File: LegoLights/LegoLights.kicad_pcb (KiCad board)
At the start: 2 copper layers, 30.5 x 7.6 mm, 4 parts, among them J1 Conn_01x02, J2 Conn_01x02

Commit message: Update paths more thick
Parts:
- moved D1 1.02 mm to (133.9, 60.5)
- moved R1 0.51 mm to (137.2, 58.3)
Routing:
- net GND: track 20.6 -> 0.01 mm
- added copper zone on F.Cu, net GND
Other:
- board text added: "Lego Lights Rev1.0"
- board text removed: "Lego Lights"
- board text removed: "Rick Winters 2024"
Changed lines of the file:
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@@
   )
   (footprint "LED_SMD:LED_1210_3225Metric_Pad1.42x2.65mm_HandSolder" (layer "F.Cu")
-    (at 133.858 59.4725 90)
+    (at 133.858 60.4885 90)
     (descr "LED SMD 1210 (3225 Metric), square (rectangular) end terminal, IPC_7351 nominal, (Body size source: http://www.tortai-tech.com/upload/download/2011102023233369053.pdf), generated with kicad-footprint-generator")
     (tags "LED handsolder")
@@
     (property "ki_keywords" "LED diode")
     (attr smd)
-    (fp_text reference "D1" (at 0 -2.28 90) (layer "F.SilkS")
+    (fp_text reference "D1" (at 0 -2.54 180) (layer "F.SilkS")
         (effects (font (size 1 1) (thickness 0.15)))
     )
@@
   )
   (footprint "Resistor_SMD:R_0805_2012Metric" (layer "F.Cu")
-    (at 137.16 58.7775 -90)
+    (at 137.16 58.2695 -90)
     (descr "Resistor SMD 0805 (2012 Metric), square (rectangular) end terminal, IPC_7351 nominal, (Body size source: IPC-SM-782 page 72, https://www.pcb-3d.com/wordpress/wp-content/uploads/ipc-sm-782a_amendment_1_and_2.pdf), generated with kicad-footprint-generator")
     (tags "resistor")
@@
     (property "ki_keywords" "R res resistor")
     (attr smd)
-    (fp_text reference "R1" (at 0 -1.65 90) (layer "F.SilkS")
+    (fp_text reference "R1" (at 0 -2.032 -180) (layer "F.SilkS")
         (effects (font (size 1 1) (thickness 0.15)))
     )
@@
   (gr_rect (start 119.38 55.88) (end 149.86 63.5)
     (stroke (width 0.2) (type default)) (fill none) (layer "Edge.Cuts"))
-  (gr_text "Lego Lights" (at 139.192 57.912) (layer "B.SilkS")
-    (effects (font (size 1 1) (thickness 0.15)) (justify left bottom mirror))
-  )
-  (gr_text "Rick Winters 2024" (at 141.986 61.214) (layer "B.SilkS")
+  (gr_text "Lego Lights Rev1.0" (at 141.478 60.452) (layer "B.SilkS")
     (effects (font (size 1 1) (thickness 0.15)) (justify left bottom mirror))
   )
@@
     (effects (font (size 1 1) (thickness 0.15)) (justify left bottom))
   )
-  (gr_text "GND" (at 139.954 61.468) (layer "F.SilkS")
+  (gr_text "GND" (at 140.208 61.722) (layer "F.SilkS")
     (effects (font (size 1 1) (thickness 0.15)) (justify left bottom))
   )
-  (gr_text "+" (at 141.478 58.928) (layer "F.SilkS")
+  (gr_text "+" (at 141.224 58.928) (layer "F.SilkS")
     (effects (font (size 1 1) (thickness 0.15)) (justify left bottom))
   )
-  (gr_text "+" (at 125.73 59.182) (layer "F.SilkS")
+  (gr_text "+" (at 126.238 58.928) (layer "F.SilkS")
     (effects (font (size 1 1) (thickness 0.15)) (justify left bottom))
   )
-  (segment (start 134.693 57.985) (end 133.858 57.985) (width 0.25) (layer "F.Cu") (net 1))
-  (segment (start 136.398 59.69) (end 134.693 57.985) (width 0.25) (layer "F.Cu") (net 1))
+  (segment (start 134.039 59.182) (end 133.858 59.001) (width 1) (layer "F.Cu") (net 1))
+  (segment (start 137.16 59.182) (end 134.039 59.182) (width 1) (layer "F.Cu") (net 1))
   (segment (start 133.858 58.42) (end 134.7235 58.42) (width 0.25) (layer "F.Cu") (net 1))
   (segment (start 144.78 60.99) (end 144.77 60.98) (width 0.25) (layer "F.Cu") (net 2))
-  (segment (start 144.77 60.98) (end 124.186 60.98) (width 0.25) (layer "F.Cu") (net 2))
-  (segment (start 137.16 57.865) (end 135.937 56.642) (width 0.25) (layer "F.Cu") (net 3))
-  (segment (start 137.745 58.45) (end 137.16 57.865) (width 0.25) (layer "F.Cu") (net 3))
-  (segment (start 132.334 56.642) (end 130.536 58.44) (width 0.25) (layer "F.Cu") (net 3))
-  (segment (start 144.78 58.45) (end 137.745 58.45) (width 0.25) (layer "F.Cu") (net 3))
-  (segment (start 130.536 58.44) (end 124.186 58.44) (width 0.25) (layer "F.Cu") (net 3))
-  (segment (start 144.78 58.45) (end 144.75 58.42) (width 0.25) (layer "F.Cu") (net 3))
-  (segment (start 135.937 56.642) (end 132.334 56.642) (width 0.25) (layer "F.Cu") (net 3))
+  (segment (start 144.78 58.45) (end 143.48 57.15) (width 0.75) (layer "F.Cu") (net 3))
+  (segment (start 125.431 57.15) (end 124.181 58.4) (width 0.75) (layer "F.Cu") (net 3))
+  (segment (start 143.48 57.15) (end 125.431 57.15) (width 0.75) (layer "F.Cu") (net 3))
+  (zone (net 2) (net_name "GND") (layer "F.Cu") (hatch edge 0.5)
+    (connect_pads (clearance 0.5))
+    (min_thickness 0.25) (filled_areas_thickness no)
+    (fill yes (thermal_gap 0.5) (thermal_bridge_width 0.5))
+    (polygon
+      (pts
+        (xy 149.86 55.88)
+        (xy 119.38 55.88)
+        (xy 119.38 63.5)
+        (xy 149.86 63.5)
+        (xy 149.86 55.88)
+      )
+    )
+  )
 )

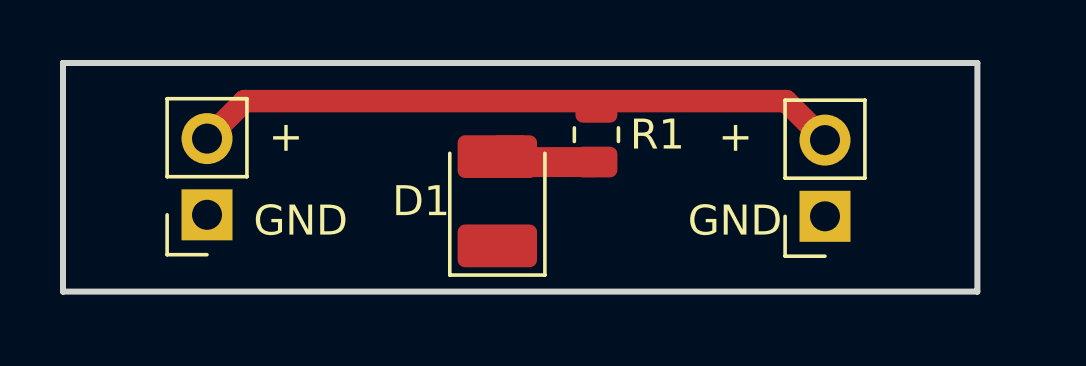
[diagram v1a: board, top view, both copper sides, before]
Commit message: Update dimensions to correct size of a lego 1x4
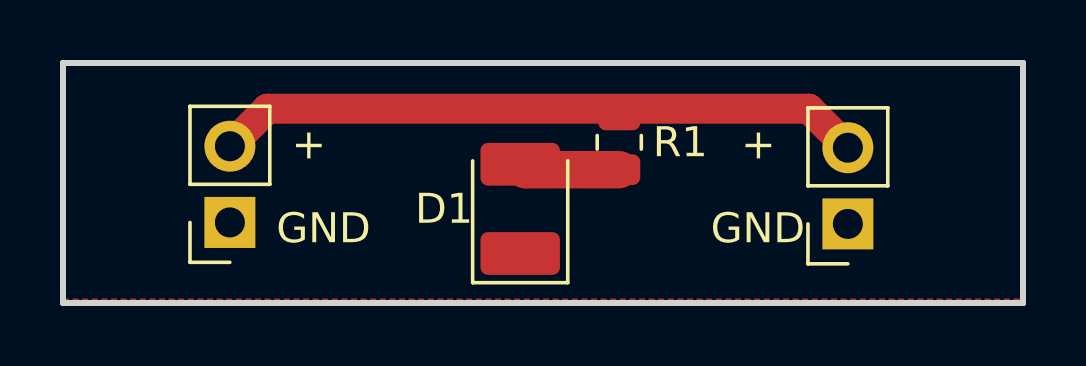
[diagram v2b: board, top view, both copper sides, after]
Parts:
- moved J1 0.80 mm to (124.9, 61.2)
- moved D1 0.80 mm to (134.6, 60.7)
- moved J2 0.80 mm to (145.5, 61.2)
- moved R1 0.80 mm to (137.9, 58.5)
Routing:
- net Net-(D1-A): track 4.24 -> 3.38 mm
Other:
- board size 30.5 x 7.6 mm -> 32 x 8 mm
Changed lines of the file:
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@@
   (net 3 "+12V")
   (footprint "Connector_PinSocket_2.54mm:PinSocket_1x02_P2.54mm_Vertical" (layer "F.Cu")
-    (at 124.181 60.94 180)
+    (at 124.943 61.194 180)
     (descr "Through hole straight socket strip, 1x02, 2.54mm pitch, single row (from Kicad 4.0.7), script generated")
     (tags "Through hole socket strip THT 1x02 2.54mm single row")
@@
   )
   (footprint "LED_SMD:LED_1210_3225Metric_Pad1.42x2.65mm_HandSolder" (layer "F.Cu")
-    (at 133.858 60.4885 90)
+    (at 134.62 60.7425 90)
     (descr "LED SMD 1210 (3225 Metric), square (rectangular) end terminal, IPC_7351 nominal, (Body size source: http://www.tortai-tech.com/upload/download/2011102023233369053.pdf), generated with kicad-footprint-generator")
     (tags "LED handsolder")
@@
   )
   (footprint "Resistor_SMD:R_0805_2012Metric" (layer "F.Cu")
-    (at 137.16 58.2695 -90)
+    (at 137.922 58.5235 -90)
     (descr "Resistor SMD 0805 (2012 Metric), square (rectangular) end terminal, IPC_7351 nominal, (Body size source: IPC-SM-782 page 72, https://www.pcb-3d.com/wordpress/wp-content/uploads/ipc-sm-782a_amendment_1_and_2.pdf), generated with kicad-footprint-generator")
     (tags "resistor")
@@
   )
   (footprint "Connector_PinSocket_2.54mm:PinSocket_1x02_P2.54mm_Vertical" (layer "F.Cu")
-    (at 144.78 60.99 180)
+    (at 145.542 61.244 180)
     (descr "Through hole straight socket strip, 1x02, 2.54mm pitch, single row (from Kicad 4.0.7), script generated")
     (tags "Through hole socket strip THT 1x02 2.54mm single row")
@@
     )
   )
-  (gr_rect (start 119.38 55.88) (end 149.86 63.5)
+  (gr_rect (start 119.38 55.88) (end 151.38 63.88)
     (stroke (width 0.2) (type default)) (fill none) (layer "Edge.Cuts"))
-  (gr_text "Lego Lights Rev1.0" (at 141.478 60.452) (layer "B.SilkS")
+  (gr_text "Lego Lights Rev1.0" (at 142.24 60.706) (layer "B.SilkS")
     (effects (font (size 1 1) (thickness 0.15)) (justify left bottom mirror))
   )
-  (gr_text "GND" (at 125.73 61.722) (layer "F.SilkS")
-    (effects (font (size 1 1) (thickness 0.15)) (justify left bottom))
-  )
-  (gr_text "GND" (at 140.208 61.722) (layer "F.SilkS")
-    (effects (font (size 1 1) (thickness 0.15)) (justify left bottom))
-  )
-  (gr_text "+" (at 141.224 58.928) (layer "F.SilkS")
-    (effects (font (size 1 1) (thickness 0.15)) (justify left bottom))
-  )
-  (gr_text "+" (at 126.238 58.928) (layer "F.SilkS")
-    (effects (font (size 1 1) (thickness 0.15)) (justify left bottom))
-  )
-  (segment (start 134.039 59.182) (end 133.858 59.001) (width 1) (layer "F.Cu") (net 1))
-  (segment (start 137.16 59.182) (end 134.039 59.182) (width 1) (layer "F.Cu") (net 1))
-  (segment (start 133.858 58.42) (end 134.7235 58.42) (width 0.25) (layer "F.Cu") (net 1))
-  (segment (start 144.78 60.99) (end 144.77 60.98) (width 0.25) (layer "F.Cu") (net 2))
-  (segment (start 144.78 58.45) (end 143.48 57.15) (width 0.75) (layer "F.Cu") (net 3))
-  (segment (start 125.431 57.15) (end 124.181 58.4) (width 0.75) (layer "F.Cu") (net 3))
-  (segment (start 143.48 57.15) (end 125.431 57.15) (width 0.75) (layer "F.Cu") (net 3))
+  (gr_text "GND" (at 126.492 61.976) (layer "F.SilkS")
+    (effects (font (size 1 1) (thickness 0.15)) (justify left bottom))
+  )
+  (gr_text "GND" (at 140.97 61.976) (layer "F.SilkS")
+    (effects (font (size 1 1) (thickness 0.15)) (justify left bottom))
+  )
+  (gr_text "+" (at 141.986 59.182) (layer "F.SilkS")
+    (effects (font (size 1 1) (thickness 0.15)) (justify left bottom))
+  )
+  (gr_text "+" (at 127 59.182) (layer "F.SilkS")
+    (effects (font (size 1 1) (thickness 0.15)) (justify left bottom))
+  )
+  (segment (start 134.801 59.436) (end 134.62 59.255) (width 1.25) (layer "F.Cu") (net 1))
+  (segment (start 137.922 59.436) (end 134.801 59.436) (width 1.25) (layer "F.Cu") (net 1))
+  (segment (start 145.542 58.704) (end 144.242 57.404) (width 1) (layer "F.Cu") (net 3))
+  (segment (start 126.193 57.404) (end 124.943 58.654) (width 1) (layer "F.Cu") (net 3))
+  (segment (start 144.242 57.404) (end 126.193 57.404) (width 1) (layer "F.Cu") (net 3))
   (zone (net 2) (net_name "GND") (layer "F.Cu") (hatch edge 0.5)
     (connect_pads (clearance 0.5))
@@
     (polygon
       (pts
-        (xy 149.86 55.88)
+        (xy 151.384 55.88)
         (xy 119.38 55.88)
-        (xy 119.38 63.5)
-        (xy 149.86 63.5)
-        (xy 149.86 55.88)
+        (xy 119.38 63.754)
+        (xy 151.384 63.754)
       )
     )
